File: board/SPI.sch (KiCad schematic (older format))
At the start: 39 parts, among them P14 CONN_5X2, P28 CONN_8, P3 CONN_7X2, U11 MICRO_SD, U17 FXO-HC536R, U26 CB3LV-3I-27M0000, U3 W25Q128FVEIG

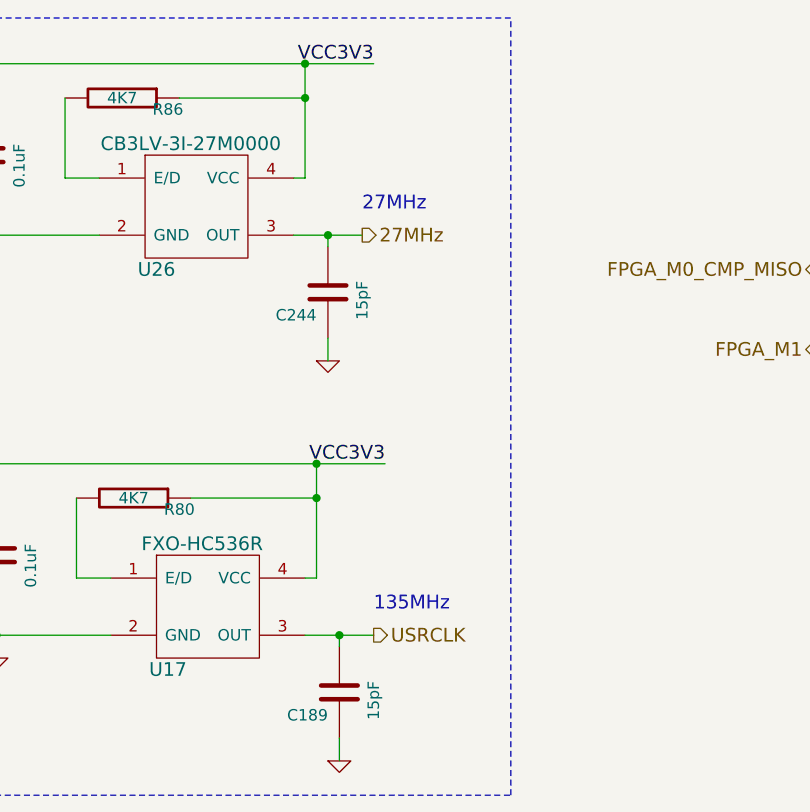
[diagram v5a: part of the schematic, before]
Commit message: Fixing issue with clock labeling.
Fixes #42.
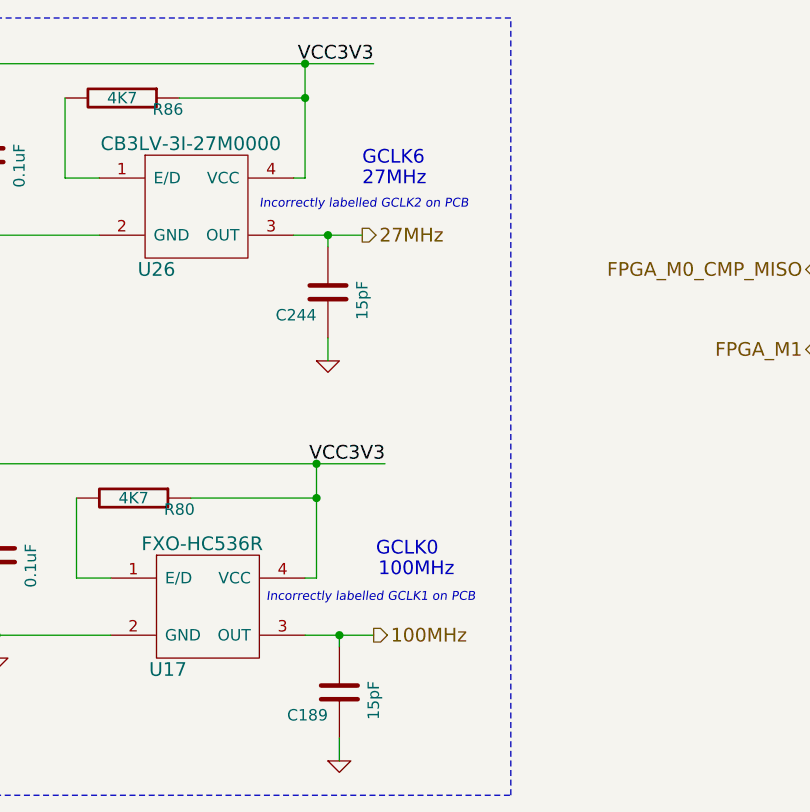
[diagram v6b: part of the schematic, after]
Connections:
- net USRCLK renamed 100MHz
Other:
- note added: "100MHz"
- note added: "GCLK0"
- note added: "GCLK6"
- note added: "Incorrectly labelled GCLK1 on PCB"
- note added: "Incorrectly labelled GCLK2 on PCB"
- note removed: "135MHz"
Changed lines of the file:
@@
 VCC3V3
 Text HLabel 2550 3300 2    60   Output ~ 0
-USRCLK
+100MHz
 $Comp
 L C C189
@@
 	0    1    1    0
 $EndComp
-Text Notes 2550 3200 0    60   ~ 0
-135MHz
+Text Notes 2570 3050 0    60   ~ 0
+100MHz
 $Comp
 L FXO-HC536R U26
@@
 	1    0    0    -1
 $EndComp
-Text Notes 2500 1450 0    60   ~ 0
+Text Notes 2500 1340 0    60   ~ 0
 27MHz
 $Comp
@@
 Wire Wire Line
 	7400 1900 7600 1900
+Text Notes 2560 2960 0    60   ~ 0
+GCLK0
+Text Notes 2500 1250 0    60   ~ 0
+GCLK6
+Text Notes 2080 3160 0    39   Italic 0
+Incorrectly labelled GCLK1 on PCB
+Text Notes 2050 1440 0    39   Italic 0
+Incorrectly labelled GCLK2 on PCB
 $EndSCHEMATC
